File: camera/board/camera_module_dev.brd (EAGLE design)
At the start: 48.3 x 38.1 mm, 57 parts, among them IC1 74541PW, IC2 74541PW, Q1 MOSFET-NCHANNELBSS123LT1G, Q2 MOSFET-NCHANNELBSS123LT1G

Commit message: Updated to r0.1. Fixed reset problems. Should be ready for shipping
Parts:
- removed SJ12, SJ13: (no value), SparkFun-Passives:SJ_3
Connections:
- removed net N$10: IC2.1, SJ12.2
- removed net N$7: IC1.1, SJ13.2
- net +3V3: no longer SJ12.3, SJ13.3
- net GND: now also IC1.1, IC1.19, IC2.1, IC2.19; no longer SJ12.1, SJ13.1
- net N$8: now also U$2.3
- net PMOD_RESET: no longer IC1.19, IC2.19, QG1.1, U$1.A1, U$2.3, U$3.A1
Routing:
- net PMOD_RESET: track 104.9 -> 22.3 mm, vias 6 -> 2
- net +3V3: track 58.3 -> 53.3 mm
- net N$8: track 39.9 -> 43.0 mm
- net N$10: track 2.28 -> 0.00 mm
- net N$7: track 2.21 -> 0.00 mm

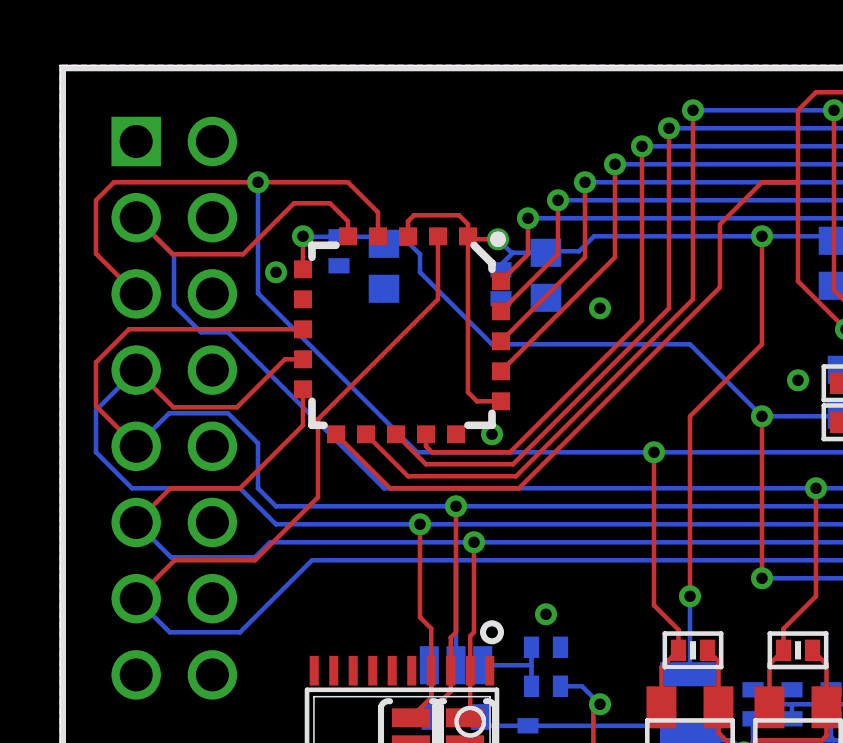
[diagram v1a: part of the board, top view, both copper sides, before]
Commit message: Fixed spacing for TCM camera pads, updated pullup resitor val on reset line
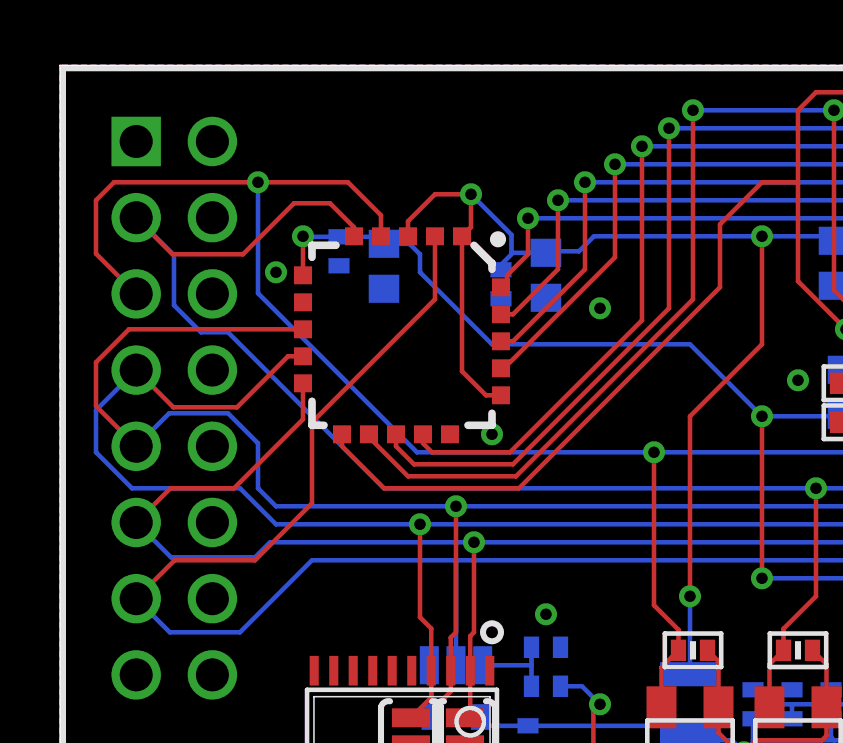
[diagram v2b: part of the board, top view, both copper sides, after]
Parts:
- R5: value 10k -> 1k
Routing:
- net N$8: track 43.0 -> 44.9 mm

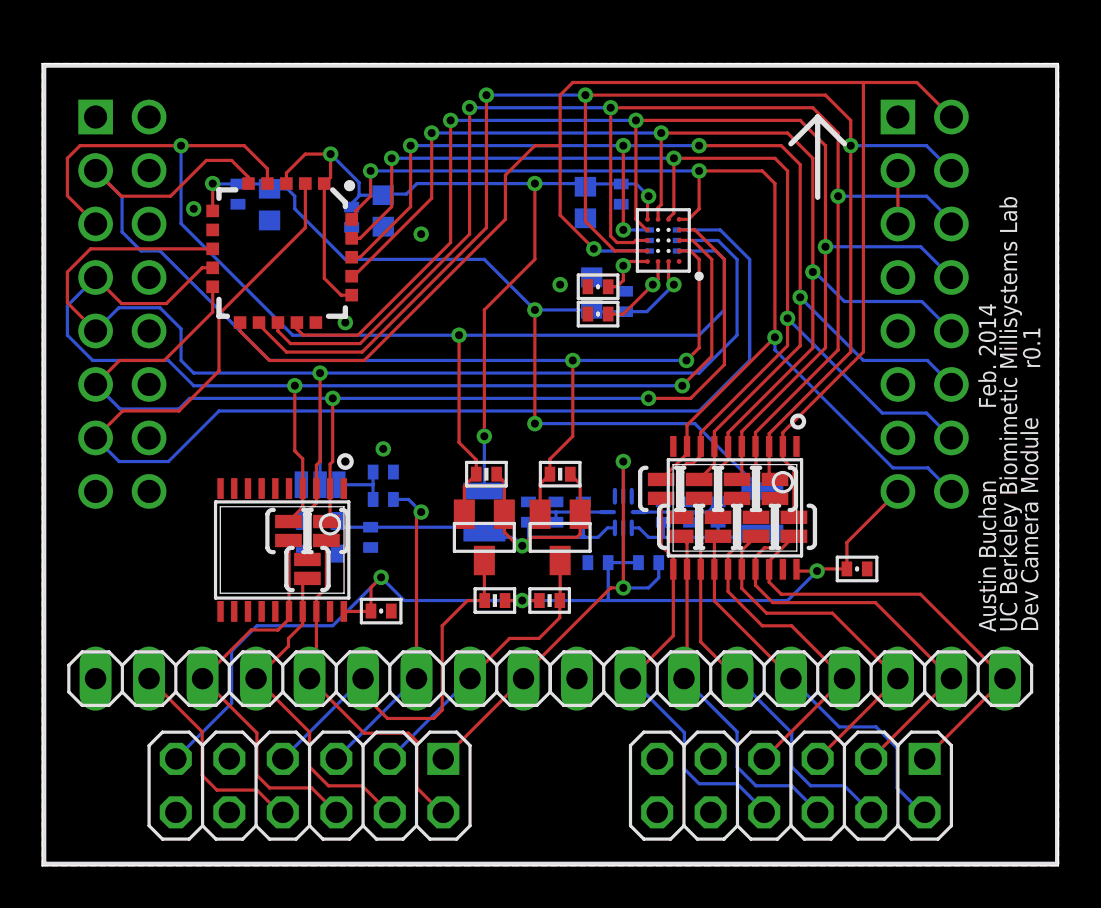
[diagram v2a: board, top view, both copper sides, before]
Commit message: Laying out smaller TCM camera board
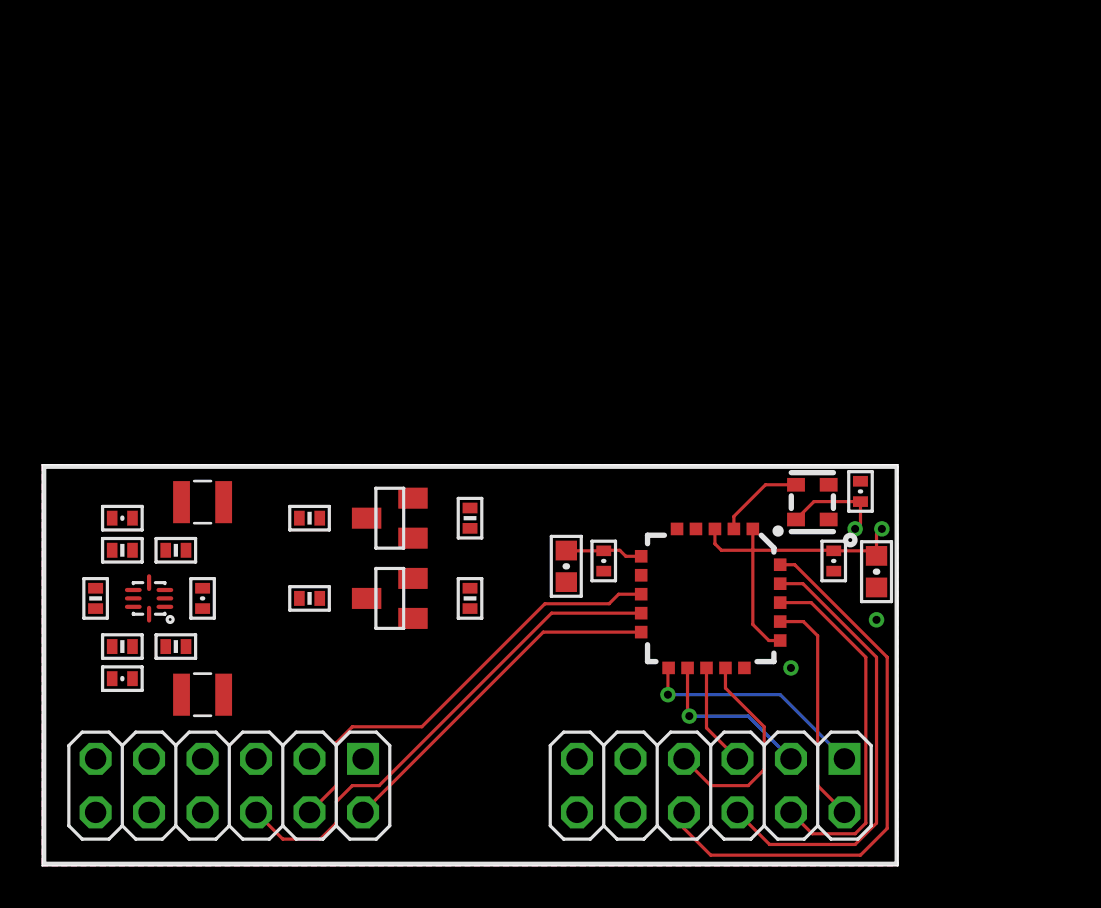
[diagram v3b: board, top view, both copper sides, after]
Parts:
- removed C10, C7: 10uF, biomimetic:0603-CAP
- removed C13, C14, C5, C6, C8, C9: 100nF, biomimetic:0402-CAP
- removed IC1, IC2: 74541PW, modular_robotics:TSSOP20
- removed JP3, JP4: (no value), pinhead:1X09
- removed R6: 2k, biomimetic:0402-RES
- removed R7: 10k, biomimetic:0402-RES
- removed SJ1, SJ10, SJ11, SJ2, SJ3, SJ4, SJ5, SJ6, SJ7, SJ8, SJ9: SOLDERJUMPERNO, SparkFun-Passives:SJ_2S-NO
- removed SJ14: (no value), SparkFun-Passives:SJ_3
- removed U$1: OVM7690-R20A-6THROUGH, modular_robotics:CSP3-20-6THROUGH
- removed U$3: OVM7690-R20A-DEV_MODULE, modular_robotics:OVM_DEV_MODULE
- R2: value 18k/5k1 -> 5k1
- moved U$7 31.6 mm to (17.8, 13.5), flipped to the bottom, turned to 0 degrees
- moved C11 29.0 mm to (39.6, 14.0), flipped to the top
- moved C15 28.1 mm to (37.6, 14.5), flipped to the top
- moved L2 28.0 mm to (7.62, 8.13), flipped to the top, turned to 90 degrees
- moved R3 27.7 mm to (3.81, 10.4), flipped to the top, turned to 180 degrees
- moved C3 26.9 mm to (3.81, 8.89), flipped to the top, turned to 180 degrees
- moved R2 26.5 mm to (6.35, 10.4), flipped to the top, turned to 180 degrees
- moved R5 26.3 mm to (2.54, 12.7), flipped to the top, turned to 90 degrees
- moved U$2 26.1 mm to (31.8, 12.7)
- moved C16 24.6 mm to (26.7, 14.5), flipped to the top
- moved QG1 23.4 mm to (36.6, 17.3), flipped to the top, turned to 90 degrees
- moved C4 23.4 mm to (38.9, 17.8), flipped to the top, turned to 270 degrees
- moved U$6 22.9 mm to (5.08, 12.7), flipped to the top, turned to 180 degrees
- moved C12 22.2 mm to (24.9, 14.2), flipped to the top
- moved C2 21.9 mm to (3.81, 16.5), flipped to the top, turned to 180 degrees
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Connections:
- removed net AVDD: U$3.A9
- removed net D0: IC1.2, SJ1.2, U$1.B3, U$2.11, U$3.B9
- removed net D1: IC1.3, SJ2.2, U$1.B4, U$2.12, U$3.B10
- removed net D2: IC1.4, SJ3.2, U$1.C4, U$2.13, U$3.B11
- removed net D3: IC1.5, SJ4.2, U$1.D4, U$2.14, U$3.B12
- removed net D4: IC1.6, SJ5.2, U$1.E3, U$2.17, U$3.B13
- removed net D5: IC1.7, SJ6.2, U$1.D3, U$2.18, U$3.B14
- removed net D6: IC1.8, SJ7.2, U$1.E2, U$2.19, U$3.B15
- removed net D7: IC1.9, SJ8.2, U$1.E1, U$2.20, U$3.B16
- removed net HSYNC: IC2.4, SJ11.2, U$1.C1, U$2.9, U$3.A4
- removed net N$1: QG1.3, SJ14.3
- removed net N$3: R6.1, R7.2, SJ14.1
- removed net N$4: C13.1, U$1.A3
- removed net N$5: C9.1, U$1.A4
- removed net PCLK: IC2.2, SJ9.2, U$1.D1, U$2.10, U$3.A6
- removed net V: U$3.A10, U$3.A11
- removed net VSYNC: IC2.3, SJ10.2, U$1.C2, U$2.8, U$3.A5
- net +3V3: no longer C5.2, C6.2, IC1.20, IC2.20, U$3.A16
- net GND: no longer C10.2, C13.2, C14.1, C5.1, C6.1, C7.1, C8.2, C9.2, IC1.1, IC1.10, IC1.19, IC2.1, IC2.10, IC2.19, IC2.5, IC2.6, IC2.7, IC2.8, IC2.9, JP3.9, JP4.9, R7.1, U$1.C3, U$3.B8
- net N$2: no longer JP3.8
- net N$6: no longer C14.2, C7.2, U$1.A2
- net N$8: no longer C10.1, C8.1, U$1.E4
- net PMOD_D0: now also U$2.11; no longer IC1.18, JP4.1, SJ1.1
- net PMOD_D1: now also U$2.12; no longer IC1.17, JP4.2, SJ2.1
- net PMOD_D2: now also U$2.13; no longer IC1.16, JP4.3, SJ3.1
- net PMOD_D3: now also U$2.14; no longer IC1.15, JP4.4, SJ4.1
- net PMOD_D4: now also U$2.17; no longer IC1.14, JP4.5, SJ5.1
- net PMOD_D5: now also U$2.18; no longer IC1.13, JP4.6, SJ6.1
- net PMOD_D6: now also U$2.19; no longer IC1.12, JP4.7, SJ7.1
- net PMOD_D7: now also U$2.20; no longer IC1.11, JP4.8, SJ8.1
- net PMOD_HSYNC: now also U$2.9; no longer IC2.16, JP3.7, SJ11.1
- net PMOD_PCLK: now also U$2.10; no longer IC2.18, JP3.5, SJ9.1
- net PMOD_RESET: no longer JP3.1
- net PMOD_SCL: no longer JP3.4
- net PMOD_SDA: no longer JP3.2
- net PMOD_VSYNC: now also U$2.8; no longer IC2.17, JP3.6, SJ10.1
- net PMOD_XCLK: no longer JP3.3, R6.2
- net SCL: no longer U$1.B2, U$3.A3
- net SDA: no longer U$1.B1, U$3.A2
- net XCLK: now also QG1.3; no longer SJ14.2, U$1.D2, U$3.A7
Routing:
- net D0: track 74.2 -> 0.00 mm, vias 1 -> 0
- net D1: track 71.7 -> 0.00 mm, vias 3 -> 0
- net D2: track 69.8 -> 0.00 mm, vias 3 -> 0
- net D3: track 63.3 -> 0.00 mm, vias 3 -> 0
- net SCL: track 60.7 -> 0.00 mm, vias 2 -> 0
- net VSYNC: track 60.5 -> 0.00 mm, vias 1 -> 0
- net XCLK: track 63.6 -> 4.17 mm
- net D4: track 58.0 -> 0.00 mm, vias 3 -> 0
- net D5: track 56.7 -> 0.00 mm, vias 5 -> 0
- net D6: track 56.1 -> 0.00 mm, vias 3 -> 0
- net SDA: track 56.0 -> 0.00 mm, vias 2 -> 0
- net HSYNC: track 55.7 -> 0.00 mm, vias 2 -> 0
- net +3V3: track 53.3 -> 0.00 mm, vias 3 -> 0
- net D7: track 53.1 -> 0.00 mm, vias 3 -> 0
- net PCLK: track 53.1 -> 0.00 mm, vias 2 -> 0
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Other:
- board size 48.3 x 38.1 mm -> 40.6 x 19.1 mm

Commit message: Finished routing, silkscreen done, ready for panelization
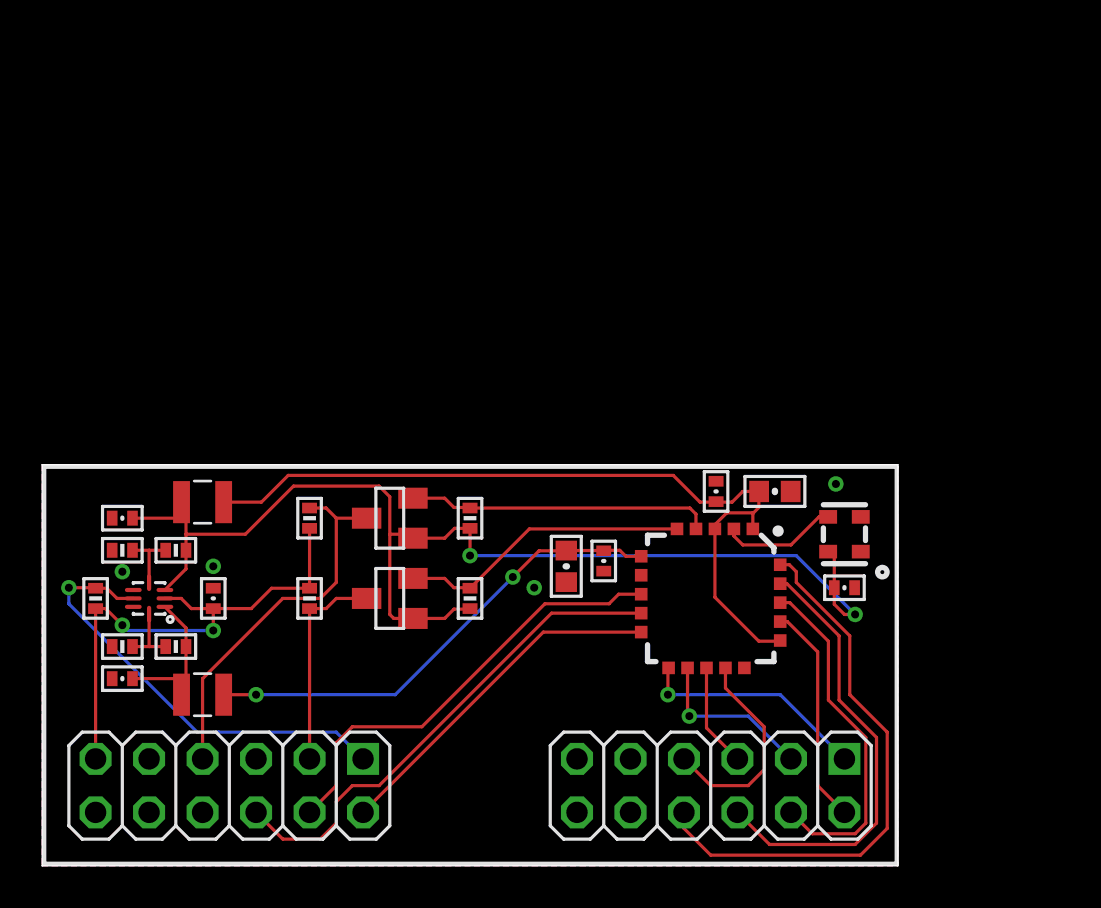
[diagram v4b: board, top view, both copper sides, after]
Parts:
- moved U$7 20.1 mm to (37.8, 13.5)
- moved C15 6.49 mm to (32.0, 17.8), turned to 270 degrees
- moved C11 6.15 mm to (34.8, 17.8), turned to 180 degrees
- moved C4 4.64 mm to (38.1, 13.2), turned to 180 degrees
- moved QG1 2.16 mm to (38.1, 15.7)
- moved C1 0.51 mm to (8.13, 12.7)
- turned R11 to 270 degrees
- turned R9 to 90 degrees
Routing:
- net VCCIO: track 4.81 -> 56.6 mm, vias 1 -> 2
- net +3V3: track 0.00 -> 24.5 mm, vias 0 -> 2
- net N$8: track 16.2 -> 38.1 mm, vias 1 -> 0
- net PMOD_RESET: track 0.00 -> 21.1 mm, vias 0 -> 1
- net N$6: track 3.69 -> 22.8 mm, vias 0 -> 2
- net PMOD_SCL: track 0.00 -> 18.0 mm
- net SCL: track 0.00 -> 14.5 mm
- net SDA: track 0.00 -> 13.9 mm
- net PMOD_SDA: track 0.00 -> 10.0 mm
- net VDD: track 0.00 -> 7.22 mm
- net N$19: track 0.00 -> 3.11 mm
- net N$21: track 0.00 -> 3.11 mm
- net XCLK: track 4.17 -> 5.54 mm
- net PMOD_D5: track 17.2 -> 16.6 mm
